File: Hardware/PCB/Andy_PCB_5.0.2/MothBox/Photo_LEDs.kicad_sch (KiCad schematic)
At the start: 71 parts, among them Q3 YJQ10N2A, Q7 YJQ10N2A

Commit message: updating for v5.0.2
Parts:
- added LED49, LED50, LED51, LED52, LED53, LED54: XL-5730UWC-05, MothBox_footprints_Library:LED-SMD_3P-L5.7-W3.0-RD, symbol MothBox_Symbol_Library:XL-5730UWC-05
- added R28, R37: 18R, MothBox_footprints_Library:R_1210_3225Metric, symbol MothBox_Symbol_Library:R_Small
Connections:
- net +12V: now also R28.1, R37.1
- net at LED12.1 (K), LED15.1 (K), LED18.1 (K)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: now also LED51.1 (K)
- net at LED27.1 (K), LED30.1 (K), LED33.1 (K)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: now also LED54.1 (K)
- new net: LED50.1 (K), LED51.2 (A)
- new net: LED49.2 (A), R28.2
- new net: LED53.1 (K), LED54.2 (A)
- new net: LED49.1 (K), LED50.2 (A)
- new net: LED52.1 (K), LED53.2 (A)
- new net: LED52.2 (A), R37.2
- no-connect marks 47 -> 62
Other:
- note added: "v5.0.1+ used the XL-2835UWC-02 it should draw around 133mA at 12V therefore each bank should draw 1.072A, or 2.144A total"
- note removed: "v5.0.1 used the XL-2835UWC-02 it should draw around 133mA at 12V therefore each bank should draw 1.072A, or 2.144A total"
- moved on the sheet: LED1, LED10, LED11, LED12, LED13, LED14, LED15, LED16, LED17, LED18, LED19, LED2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

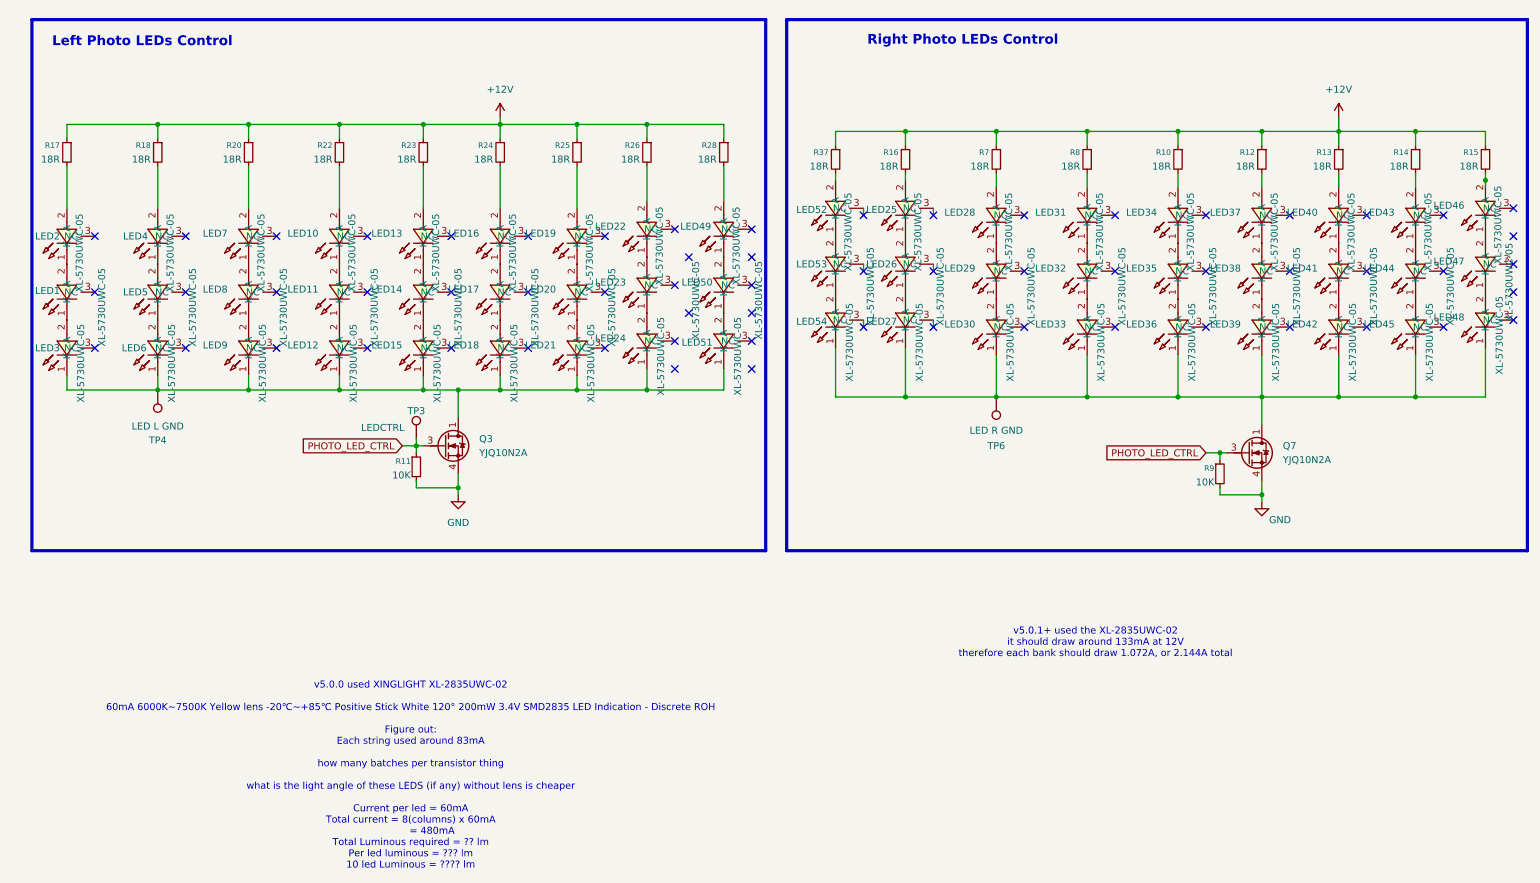
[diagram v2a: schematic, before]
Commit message: small cosmetic changes to PCB and updated Text files with current measurements from v5.0.1b testing
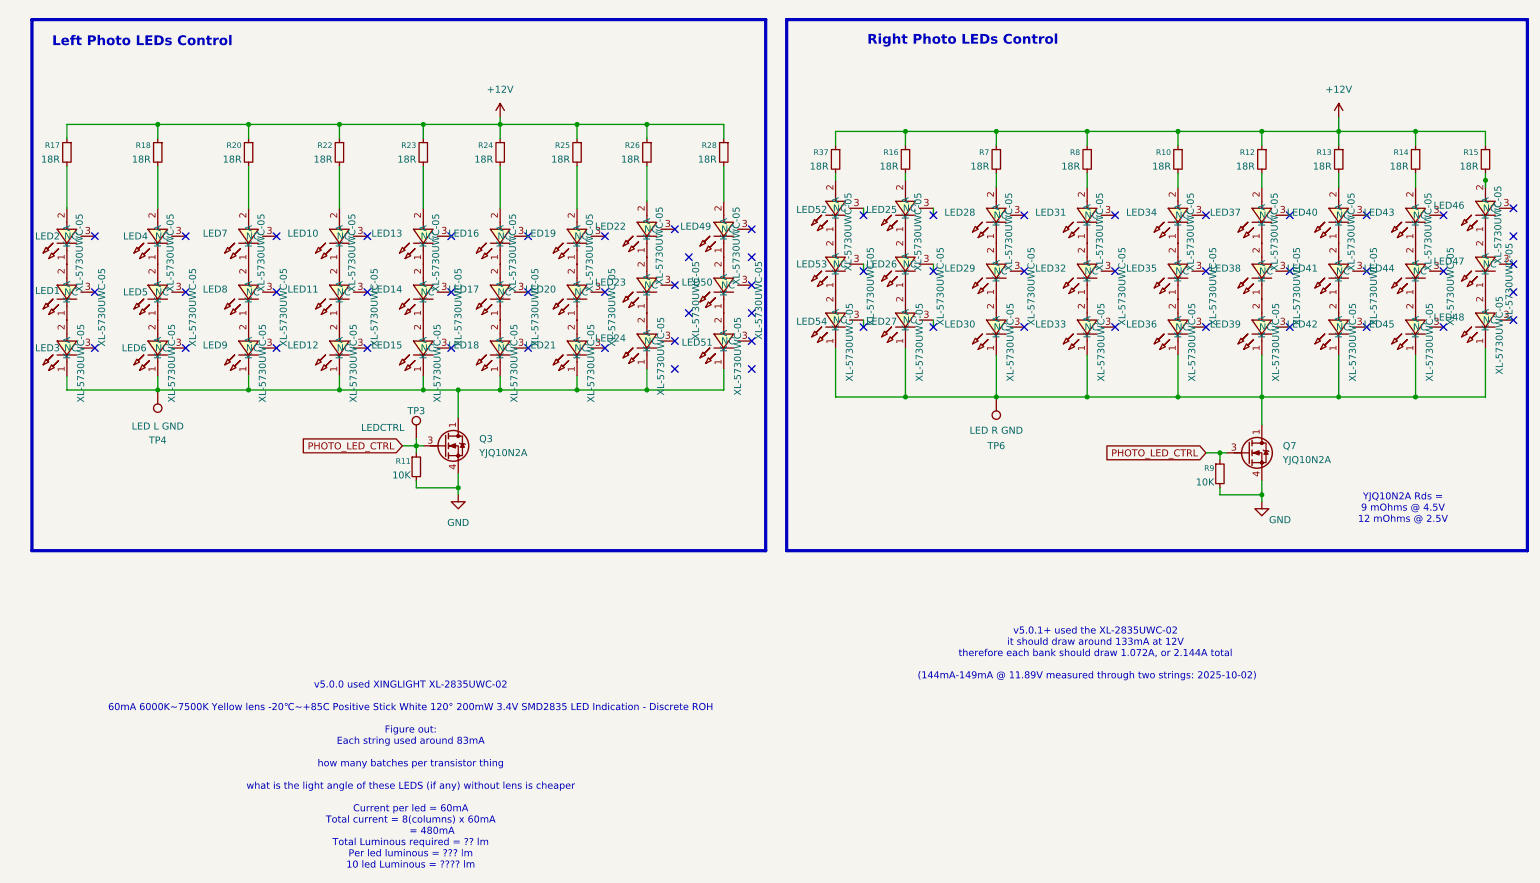
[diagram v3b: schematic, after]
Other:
- note added: "(144mA-149mA @ 11.89V measured through two strings: 2025-10-02)"
- note added: "YJQ10N2A Rds = 9 mOhms @ 4.5V 12 mOhms @ 2.5V"
- note added: "v5.0.0 used XINGLIGHT XL-2835UWC-02 60mA 6000K~7500K Yellow lens -20℃~+85C Positive Stick White 120° 200mW 3.4V SMD2835 LED Indication - Discrete ROH Figure out: Each string used around 83mA how many batches per transistor thing what is the light angle of these LEDS (if any) without lens is cheaper Current per led = 60mA Total current = 8(columns) x 60mA = 480mA Total Luminous required = ?? lm Pe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"
- note removed: "v5.0.0 used XINGLIGHT XL-2835UWC-02 60mA 6000K~7500K Yellow lens -20℃~+85℃ Positive Stick White 120° 200mW 3.4V SMD2835 LED Indication - Discrete ROH Figure out: Each string used around 83mA how many batches per transistor thing what is the light angle of these LEDS (if any) without lens is cheaper Current per led = 60mA Total current = 8(columns) x 60mA = 480mA Total Luminous required = ?? lm Pe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"
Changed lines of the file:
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@@
 		)
 	)
-	(text "v5.0.0 used XINGLIGHT XL-2835UWC-02 \n\n60mA 6000K~7500K Yellow lens -20℃~+85℃ Positive Stick White 120° 200mW 3.4V SMD2835 LED Indication - Discrete ROH\n\nFigure out:\nEach string used around 83mA\n\nhow many batches per transistor thing\n\nwhat is the light angle of these LEDS (if any) without lens is cheaper\n\nCurrent per led = 60mA\nTotal current = 8(columns) x 60mA\n			  = 480mA\nTotal Luminous required = ?? lm  \nPer led luminous = ??? lm\n10 led Luminous = ???? lm"
+	(text "(144mA-149mA @ 11.89V measured through two strings: 2025-10-02)"
+		(exclude_from_sim no)
+		(at 205.74 156.21 0)
+		(effects
+			(font
+				(size 1.27 1.27)
+			)
+		)
+	)
+	(text "v5.0.0 used XINGLIGHT XL-2835UWC-02 \n\n60mA 6000K~7500K Yellow lens -20℃~+85C Positive Stick White 120° 200mW 3.4V SMD2835 LED Indication - Discrete ROH\n\nFigure out:\nEach string used around 83mA\n\nhow many batches per transistor thing\n\nwhat is the light angle of these LEDS (if any) without lens is cheaper\n\nCurrent per led = 60mA\nTotal current = 8(columns) x 60mA\n			  = 480mA\nTotal Luminous required = ?? lm  \nPer led luminous = ??? lm\n10 led Luminous = ???? lm"
 		(exclude_from_sim no)
 		(at 82.804 174.244 0)
@@
 			)
 		)
+	)
+	(text "YJQ10N2A Rds = \n9 mOhms @ 4.5V\n12 mOhms @ 2.5V"
+		(exclude_from_sim no)
+		(at 263.144 125.73 0)
+		(effects
+			(font
+				(size 1.27 1.27)
+			)
+		)
